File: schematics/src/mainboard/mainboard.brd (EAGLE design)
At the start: 81.3 x 99.1 mm, 104 parts, among them IC1 LM2904, IC2 LM2904, IC3 LM2904, T1 2SC945, T3 BC546B, T4 BC546B, T5 BC546B, T6 BC546B

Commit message: Updated Schematics & Readme
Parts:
- added INT_TRG_CON: (no value), pinhead:1X03
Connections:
- net BD1_TRIGGER: now also INT_TRG_CON.1
- net BD2_TRIGGER: now also INT_TRG_CON.2
- net SD_TRIGGER: now also INT_TRG_CON.3
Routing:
- net SD_TRIGGER: track 84.0 -> 119.0 mm
- net BD2_TRIGGER: track 20.3 -> 50.8 mm, vias 0 -> 2
- net BD1_TRIGGER: track 72.4 -> 76.2 mm, vias 1 -> 2
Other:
- board text added: "BD1"
- board text added: "BD2"
- board text added: "SD"
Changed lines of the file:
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@@
 <wire x1="42.545" y1="59.055" x2="42.545" y2="45.085" width="0.4064" layer="25" style="shortdash"/>
 <wire x1="42.545" y1="45.085" x2="48.895" y2="38.735" width="0.4064" layer="25" style="shortdash"/>
-<wire x1="46.99" y1="71.12" x2="40.64" y2="77.47" width="0.4064" layer="25" style="shortdash"/>
-<wire x1="40.64" y1="77.47" x2="37.465" y2="77.47" width="0.4064" layer="25" style="shortdash"/>
-<wire x1="37.465" y1="77.47" x2="36.195" y2="76.2" width="0.4064" layer="25" style="shortdash"/>
+<wire x1="46.99" y1="71.12" x2="43.18" y2="71.12" width="0.4064" layer="25" style="shortdash"/>
+<wire x1="43.18" y1="71.12" x2="41.91" y2="72.39" width="0.4064" layer="25" style="shortdash"/>
+<wire x1="41.91" y1="72.39" x2="41.91" y2="74.93" width="0.4064" layer="25" style="shortdash"/>
+<wire x1="41.91" y1="74.93" x2="40.005" y2="76.835" width="0.4064" layer="25" style="shortdash"/>
+<wire x1="40.005" y1="76.835" x2="36.83" y2="76.835" width="0.4064" layer="25" style="shortdash"/>
+<wire x1="36.83" y1="76.835" x2="36.195" y2="76.2" width="0.4064" layer="25" style="shortdash"/>
 <wire x1="36.195" y1="76.2" x2="25.4" y2="76.2" width="0.4064" layer="25" style="shortdash"/>
 <wire x1="25.4" y1="76.2" x2="21.59" y2="80.01" width="0.4064" layer="25" style="shortdash"/>
@@
 <hole x="60.96" y="61.595" drill="3.2004"/>
 <hole x="25.4" y="9.525" drill="3.2004"/>
+<text x="44.45" y="80.01" size="1.27" layer="21" font="vector" rot="R180">BD1</text>
+<text x="44.45" y="77.47" size="1.27" layer="21" font="vector" rot="R180">BD2</text>
+<text x="44.45" y="74.93" size="1.27" layer="21" font="vector" rot="R180">SD</text>
 </plain>
 <attributes>
@@
 </element>
 <element name="C25" library="resistor" package="C050-024X044" value="0.056u" x="36.83" y="72.39" smashed="yes">
-<attribute name="NAME" x="40.64" y="71.755" size="1.27" layer="25" font="vector" ratio="10"/>
+<attribute name="NAME" x="29.845" y="71.755" size="1.27" layer="25" font="vector" ratio="10"/>
 <attribute name="VALUE" x="34.671" y="69.723" size="1.27" layer="27" ratio="10"/>
 </element>
@@
 <attribute name="POPULARITY" value="92" x="58.42" y="82.55" size="1.778" layer="27" rot="R90" display="off"/>
 <attribute name="VALUE" x="61.595" y="78.74" size="1.27" layer="27" rot="R90"/>
+</element>
+<element name="INT_TRG_CON" library="pinhead" library_urn="urn:adsk.eagle:library:325" package="1X03" package3d_urn="urn:adsk.eagle:package:22458/2" value="" x="46.355" y="76.835" smashed="yes" rot="R90">
+<attribute name="NAME" x="49.53" y="71.755" size="1.27" layer="25" font="vector" ratio="10" rot="R90"/>
+<attribute name="POPULARITY" value="92" x="46.355" y="76.835" size="1.778" layer="27" rot="R90" display="off"/>
+<attribute name="VALUE" x="49.53" y="73.025" size="1.27" layer="27" rot="R90"/>
 </element>
 </elements>
@@
 <via x="78.74" y="74.295" extent="1-16" drill="0.35"/>
 <via x="31.115" y="56.515" extent="1-16" drill="0.35"/>
-<via x="22.225" y="75.565" extent="1-16" drill="0.35"/>
+<via x="22.225" y="76.835" extent="1-16" drill="0.35"/>
 </signal>
 <signal name="SD_TRIGGER">
@@
 <wire x1="15.24" y1="63.5" x2="16.51" y2="62.23" width="0.4064" layer="16"/>
 <wire x1="16.51" y1="62.23" x2="17.78" y2="62.23" width="0.4064" layer="16"/>
-<wire x1="15.24" y1="86.995" x2="15.24" y2="63.5" width="0.4064" layer="16"/>
+<wire x1="15.24" y1="86.995" x2="15.24" y2="73.66" width="0.4064" layer="16"/>
+<contactref element="INT_TRG_CON" pad="3"/>
+<wire x1="15.24" y1="73.66" x2="15.24" y2="63.5" width="0.4064" layer="16"/>
+<wire x1="44.45" y1="81.28" x2="29.845" y2="81.28" width="0.4064" layer="16"/>
+<wire x1="22.225" y1="73.66" x2="15.24" y2="73.66" width="0.4064" layer="16"/>
+<wire x1="46.355" y1="79.375" x2="44.45" y2="81.28" width="0.4064" layer="16"/>
+<wire x1="29.845" y1="81.28" x2="22.225" y2="73.66" width="0.4064" layer="16"/>
 </signal>
 <signal name="N$5">
@@
 <wire x1="50.165" y1="81.28" x2="46.355" y2="85.09" width="0.4064" layer="16"/>
 <wire x1="46.355" y1="85.09" x2="34.29" y2="85.09" width="0.4064" layer="16"/>
-<wire x1="50.165" y1="36.195" x2="50.165" y2="81.28" width="0.4064" layer="16"/>
+<wire x1="50.165" y1="36.195" x2="50.165" y2="74.295" width="0.4064" layer="16"/>
 <via x="50.165" y="36.195" extent="1-16" drill="0.35"/>
+<contactref element="INT_TRG_CON" pad="1"/>
+<wire x1="50.165" y1="74.295" x2="50.165" y2="81.28" width="0.4064" layer="16"/>
+<wire x1="46.355" y1="74.295" x2="50.165" y2="74.295" width="0.4064" layer="1"/>
+<via x="50.165" y="74.295" extent="1-16" drill="0.35"/>
 </signal>
 <signal name="BD2_TRIGGER">
@@
 <contactref element="BD2_CON" pad="1"/>
 <wire x1="68.58" y1="64.77" x2="71.12" y2="67.31" width="0.4064" layer="1"/>
-<wire x1="71.12" y1="75.565" x2="73.025" y2="77.47" width="0.4064" layer="1"/>
-<wire x1="73.025" y1="77.47" x2="78.74" y2="77.47" width="0.4064" layer="1"/>
-<wire x1="71.12" y1="67.31" x2="71.12" y2="75.565" width="0.4064" layer="1"/>
+<wire x1="66.675" y1="77.47" x2="78.74" y2="77.47" width="0.4064" layer="1"/>
+<wire x1="71.12" y1="67.31" x2="71.12" y2="77.47" width="0.4064" layer="1"/>
+<wire x1="71.12" y1="77.47" x2="66.675" y2="77.47" width="0.4064" layer="1"/>
+<contactref element="INT_TRG_CON" pad="2"/>
+<wire x1="46.355" y1="76.835" x2="52.07" y2="76.835" width="0.4064" layer="1"/>
+<wire x1="52.07" y1="76.835" x2="52.705" y2="77.47" width="0.4064" layer="1"/>
+<wire x1="52.705" y1="77.47" x2="60.325" y2="77.47" width="0.4064" layer="1"/>
+<wire x1="60.325" y1="77.47" x2="66.675" y2="77.47" width="0.4064" layer="16"/>
+<via x="60.325" y="77.47" extent="1-16" drill="0.35"/>
+<via x="66.675" y="77.47" extent="1-16" drill="0.35"/>
 </signal>
 <signal name="N$58">

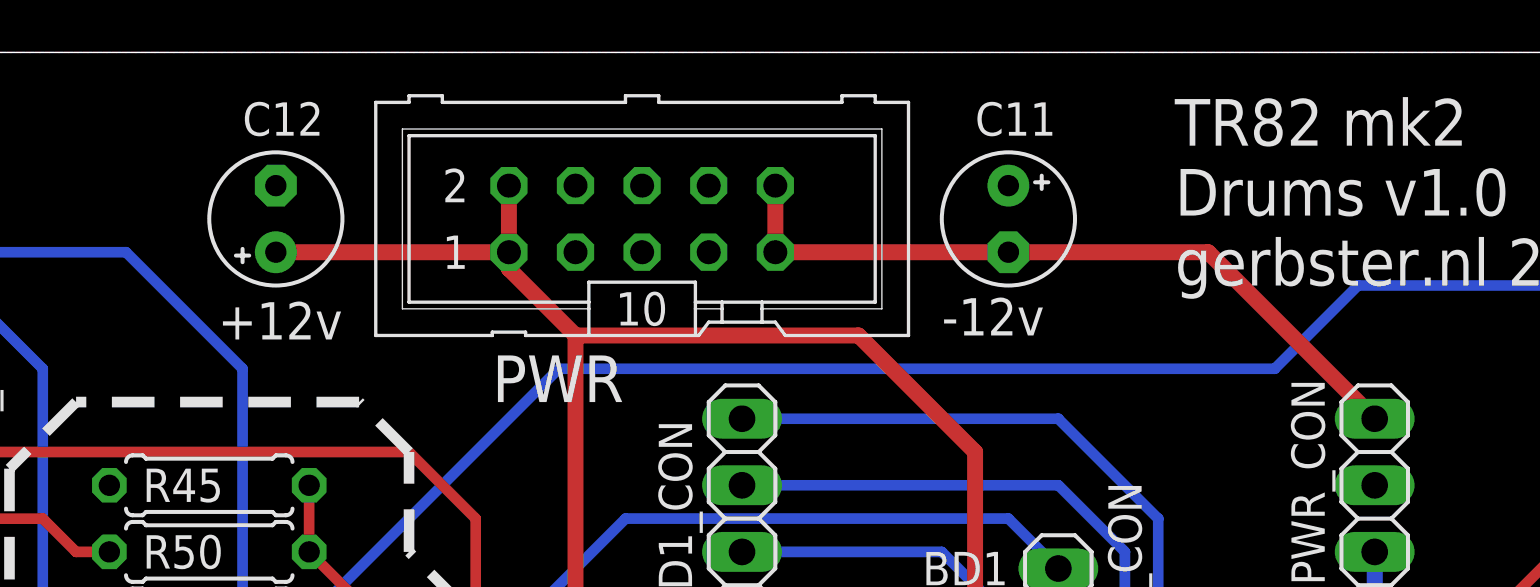
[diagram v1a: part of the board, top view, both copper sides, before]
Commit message: Updated Schematics, Fixed Power Socket orientation
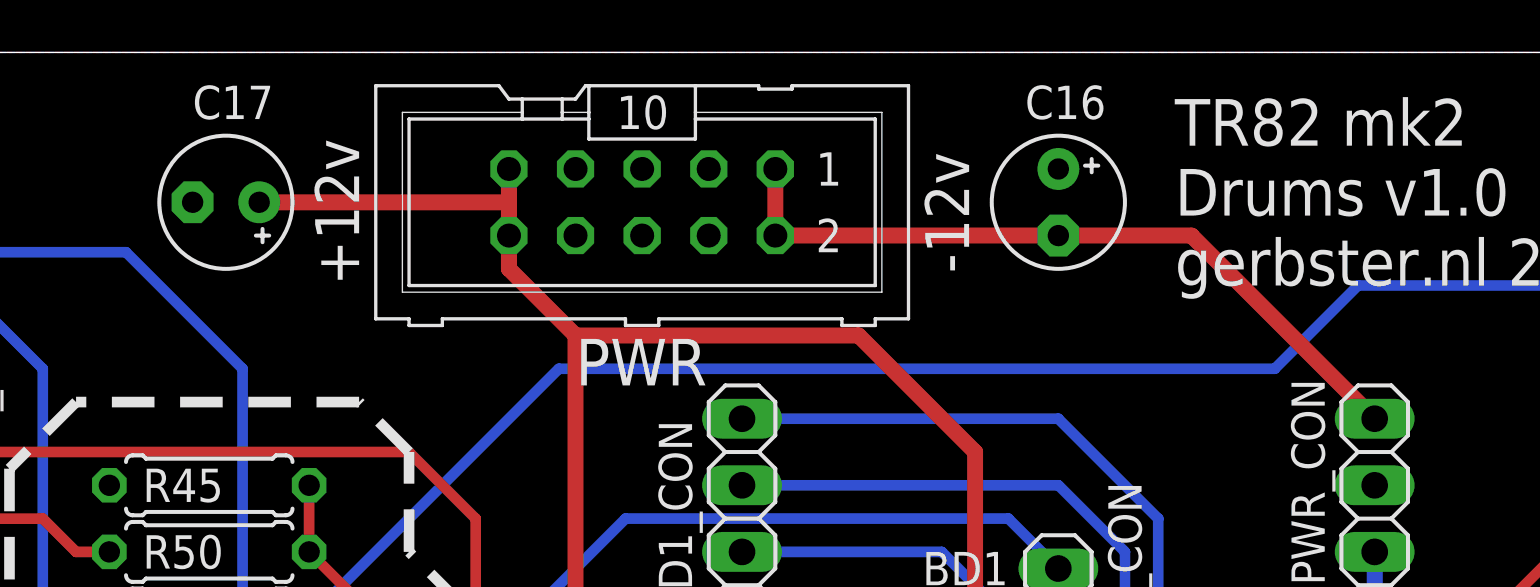
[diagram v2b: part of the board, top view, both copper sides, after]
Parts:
- removed C11, C12: 10uf, resistor:E2,5-5
- added C16, C17: 10uf, resistor:E2,5-5
- C1, C10, C19, C35: value 47u/16v -> 47uF/16v
- C13, C2, C23: value 0.47u/50v -> .47uF/50v
- C14, C15, C25: value 0.056u -> .056uF
- C18: value 33u -> 33uF
- C20, C21: value 0.027u -> .027uF
- C22: value 0.0033u -> .0033uF
- C24: value 4.7u/50v -> 4.7uF/50v
- C26: value 0.0022u -> .0022uF
- C27: value 0.047 -> .047uF
- C28: value 0.0015u -> .0015uF
- C29, C30: value 0.0018u -> .0018uF
- C3, C4: value 0.056uf -> .056uF
- C31: value 0.01u -> .01uF
- C32, C34, C7, C8: value 1u/50v -> 1uF/50v
- C33: value 22p -> 22pF
- C5, C6: value 0.015uf -> .015uF
- C9: value 0.01uf -> .01uF
- D1, D2: value 1N4148DO35-7 -> 1N4148
- moved PWR 0.64 mm to (30.5, 93.3), turned to 180 degrees
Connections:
- net +12V: now also C17.+, PWR.10, PWR.9; no longer C12.+, PWR.1, PWR.2
- net -12V: now also C16.-, PWR.1, PWR.2; no longer C11.-, PWR.10, PWR.9
- net GND: now also C16.+, C17.-; no longer C11.+, C12.-
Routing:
- net +12V: track 273.3 -> 274.6 mm
